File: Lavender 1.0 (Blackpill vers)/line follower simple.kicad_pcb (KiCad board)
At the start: 2 copper layers, 214 x 187.9 mm, 259 parts, among them J1 XT30UPB-M, J10 Conn_01x13_Pin, J11 Conn_01x13_Pin, J12 Conn_01x13_Pin, J13 Conn_01x13_Pin, J14 Conn_01x20_MountingPin, J15 Conn_01x11_Pin, J16 Conn_01x11_Pin, J17 Conn_01x11_Pin, J18 Conn_01x11_Pin, J19 Conn_01x11_Pin, J2 Conn_01x20_MountingPin, J3 Conn_01x02_Pin, J4 Conn_01x02_Pin, J5 Conn_01x28_Pin, J6 Conn_01x20_MountingPin, J7 Conn_01x20_MountingPin, J8 Conn_01x28_Pin, J9 Conn_01x20_MountingPin, Q1 BPW40, Q2 BPW40, Q3 BPW40, Q4 BPW40, Q5 BPW40, Q6 BPW40, Q7 BPW40, Q8 BPW40, Q9 BPW40, SW2 SW_Push, SW3 SW_Push, SW5 SW_Push_DPDT, SW6 SW_Push_DPDT, U1 74HC4067, U10 QRE1113GR, U11 QRE1113GR, U12 QRE1113GR, U13 QRE1113GR, U14 QRE1113GR, U15 QRE1113GR, U16 QRE1113GR, U17 QRE1113GR, U18 QRE1113GR, U19 TCRT5000L, U2 TCRT5000L, U20 TCRT5000L, U21 QRE1113GR, U22 QRE1113GR, U23 QRE1113GR, U24 QRE1113GR, U25 QRE1113GR, U26 QRE1113GR, U27 QRE1113GR, U28 QRE1113GR, U29 QRE1113GR, U30 QRE1113GR, U31 QRE1113GR, U32 QRE1113GR, U33 QRE1113GR, U34 QRE1113GR, U35 QRE1113GR, U36 QRE1113GR, U4 TCRT5000L, U5 TCRT5000L, U6 TCRT5000L, U7 TCRT5000L, U8 TCRT5000L, U9 TCRT5000L

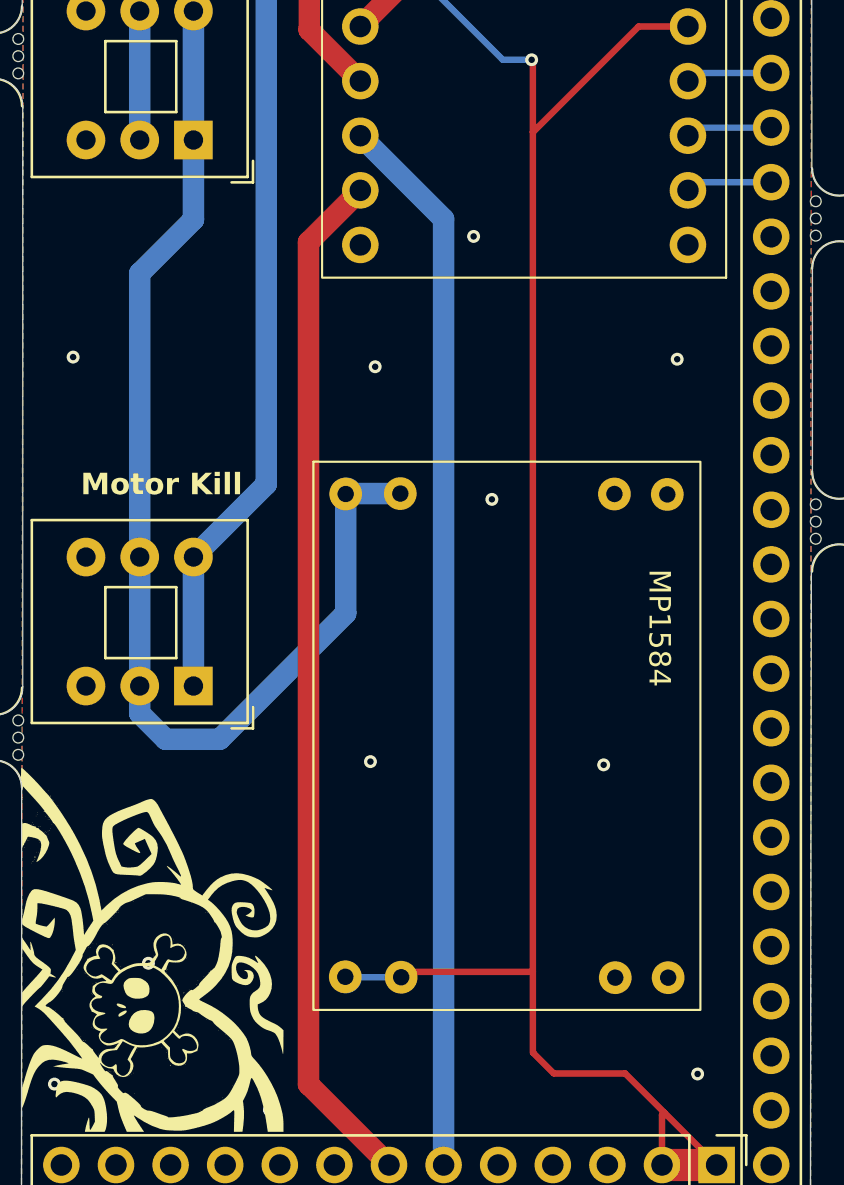
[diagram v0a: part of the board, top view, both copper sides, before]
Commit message: fix footprint
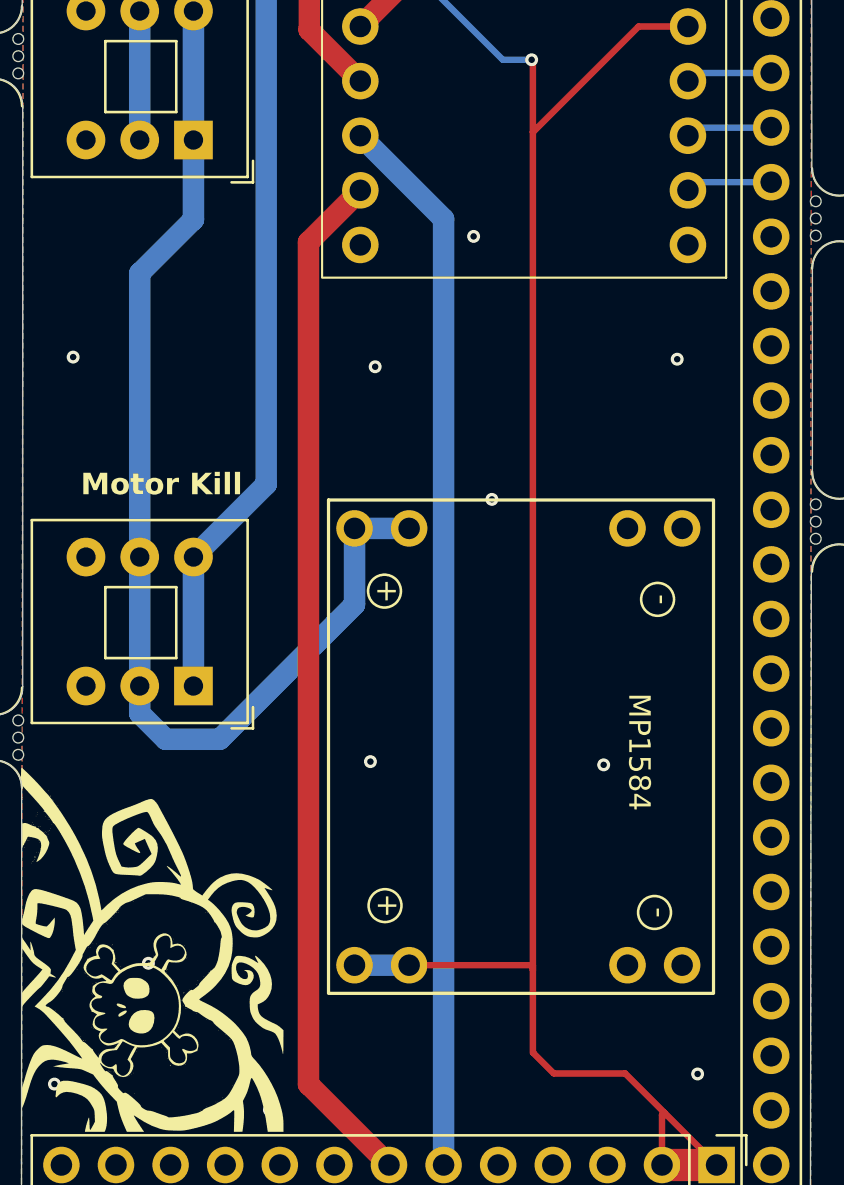
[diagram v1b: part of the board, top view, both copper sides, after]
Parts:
- moved MP1 1.27 mm to (171.2, 118.3)
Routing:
- net BAT+_out: track 54.3 -> 52.9 mm
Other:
- board text removed: "MP1584"
